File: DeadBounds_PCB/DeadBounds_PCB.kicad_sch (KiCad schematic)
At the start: 1 part

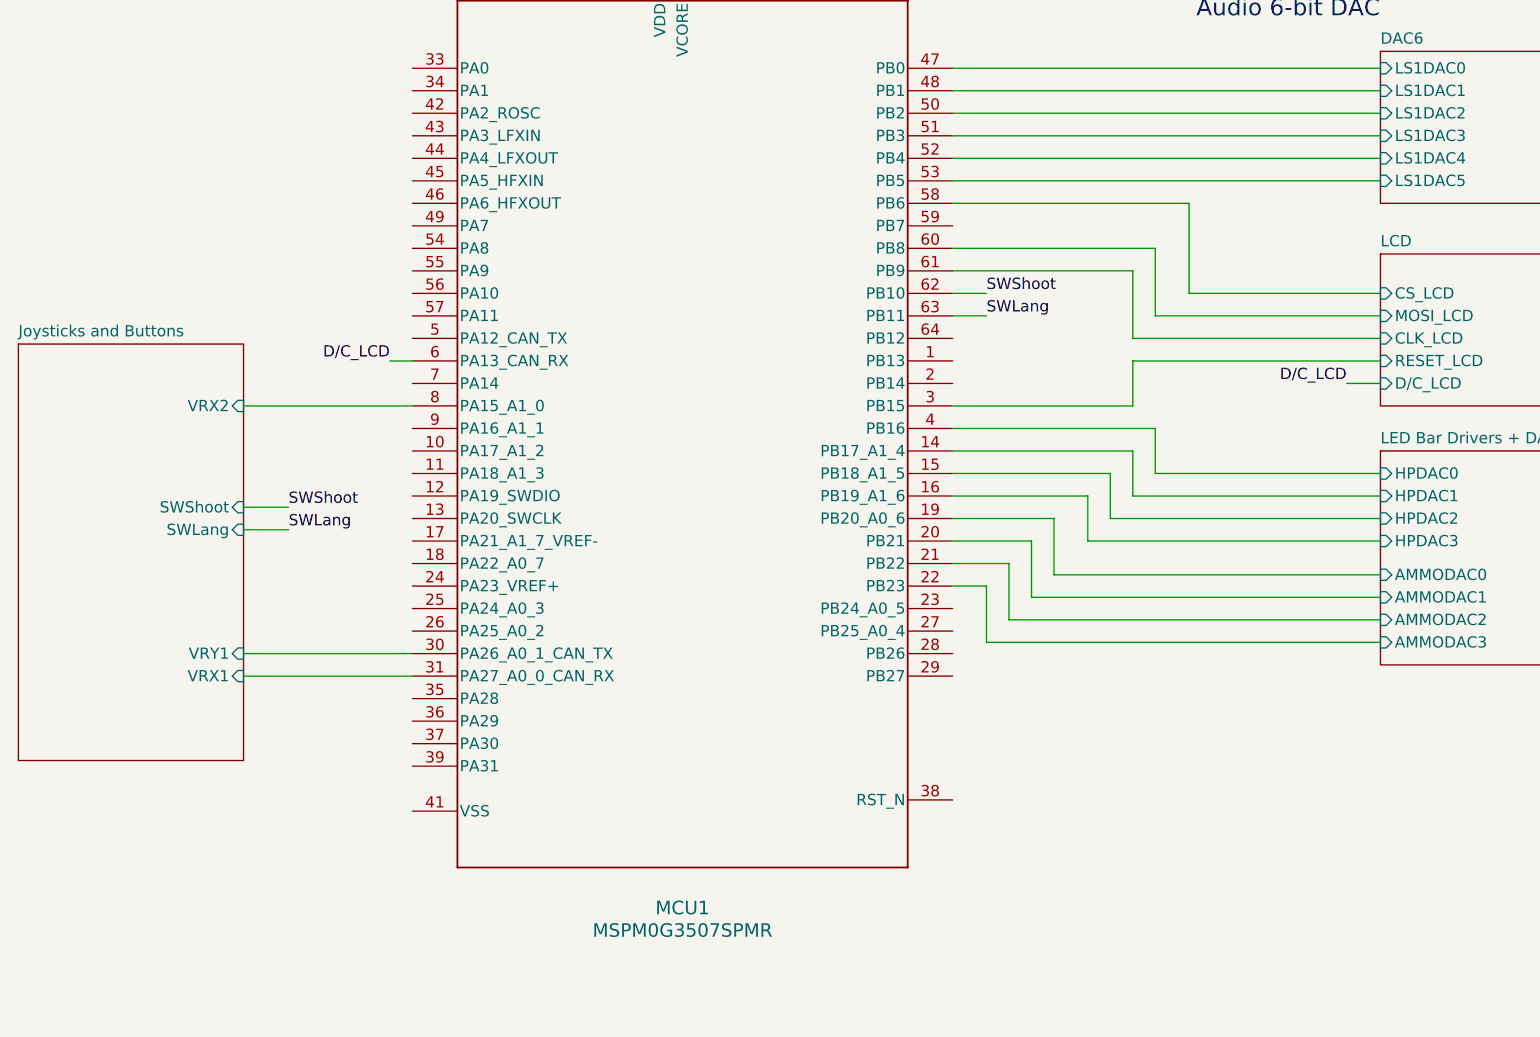
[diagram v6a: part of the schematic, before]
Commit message: Added amplifier circuit and additional jumpers to PCB
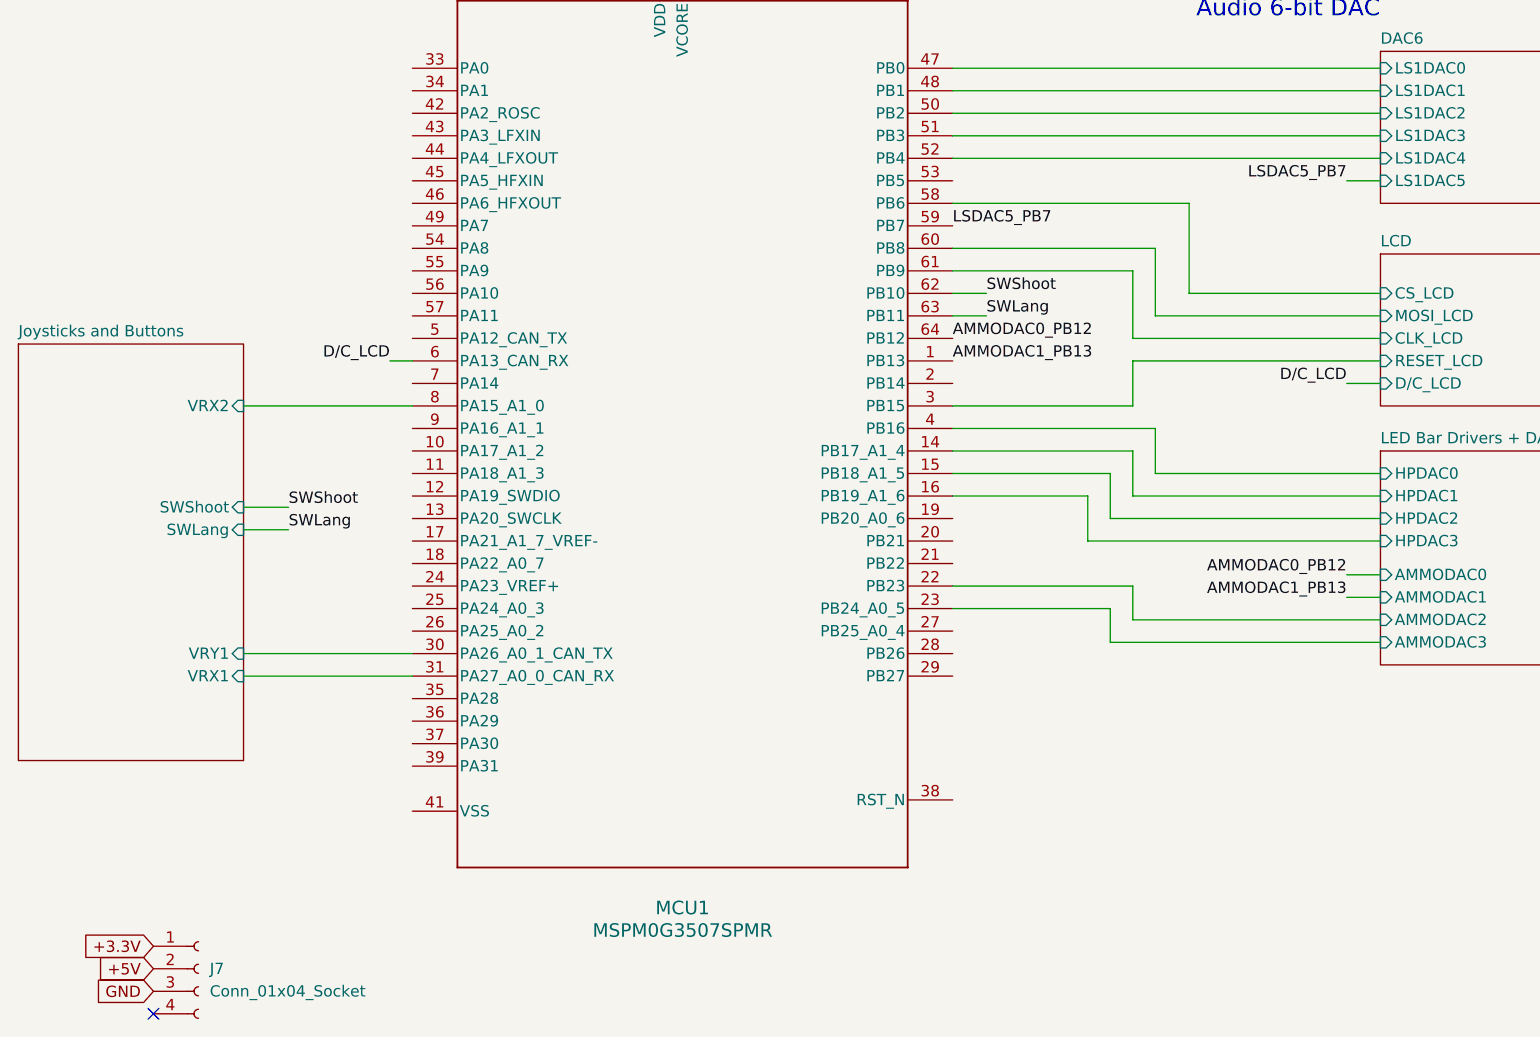
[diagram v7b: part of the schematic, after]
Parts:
- added J7: Conn_01x04_Socket, Connector_PinSocket_2.54mm:PinSocket_1x04_P2.54mm_Horizontal, symbol Connector:Conn_01x04_Socket
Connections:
- net LED Bar Drivers + DAC4s/AMMODAC2: now also MCU1.22 (PB23); no longer MCU1.21 (PB22)
- net LED Bar Drivers + DAC4s/AMMODAC3: now also MCU1.23 (PB24_A0_5); no longer MCU1.22 (PB23)
- net AMMODAC1_PB13: now reaches MCU1.1 (PB13)
- net LSDAC5_PB7: now reaches MCU1.59 (PB7)
- net AMMODAC0_PB12: now reaches MCU1.64 (PB12)
- net DAC6/LS1DAC5: no longer names the net of MCU1.53 (PB5)
- net LED Bar Drivers + DAC4s/AMMODAC0: no longer names the net of MCU1.19 (PB20_A0_6)
- net LED Bar Drivers + DAC4s/AMMODAC1: no longer names the net of MCU1.20 (PB21)
- new net +3.3V: J7.1 (Pin_1)
- new net +5V: J7.2 (Pin_2)
- new net GND: J7.3 (Pin_3)
- no-connect marks 0 -> 1
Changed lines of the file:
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@@
 		)
+	)
+	(no_connect
+		(at 137.16 149.86)
 	)
 	(wire
@@
 	(wire
 		(pts
+			(xy 247.65 105.41) (xy 275.59 105.41)
+		)
+		(stroke
+			(width 0)
+			(type default)
+		)
+	)
+	(wire
+		(pts
 			(xy 245.11 93.98) (xy 275.59 93.98)
 		)
@@
 	(wire
 		(pts
-			(xy 231.14 101.6) (xy 231.14 107.95)
-		)
-		(stroke
-			(width 0)
-			(type default)
-		)
-	)
-	(wire
-		(pts
 			(xy 245.11 88.9) (xy 245.11 93.98)
 		)
@@
 	(wire
 		(pts
-			(xy 238.76 100.33) (xy 275.59 100.33)
-		)
-		(stroke
-			(width 0)
-			(type default)
-		)
-	)
-	(wire
-		(pts
 			(xy 250.19 83.82) (xy 250.19 88.9)
 		)
@@
 	(wire
 		(pts
+			(xy 271.78 102.87) (xy 275.59 102.87)
+		)
+		(stroke
+			(width 0)
+			(type default)
+		)
+	)
+	(wire
+		(pts
 			(xy 250.19 63.5) (xy 250.19 71.12)
 		)
@@
 	(wire
 		(pts
-			(xy 236.22 102.87) (xy 275.59 102.87)
+			(xy 271.78 100.33) (xy 275.59 100.33)
 		)
 		(stroke
@@
 	(wire
 		(pts
+			(xy 247.65 105.41) (xy 247.65 101.6)
+		)
+		(stroke
+			(width 0)
+			(type default)
+		)
+	)
+	(wire
+		(pts
 			(xy 163.83 76.2) (xy 166.37 76.2)
 		)
@@
 	(wire
 		(pts
-			(xy 238.76 93.98) (xy 238.76 100.33)
-		)
-		(stroke
-			(width 0)
-			(type default)
-		)
-	)
-	(wire
-		(pts
 			(xy 231.14 68.58) (xy 227.33 68.58)
 		)
@@
 	(wire
 		(pts
-			(xy 227.33 96.52) (xy 236.22 96.52)
+			(xy 245.11 104.14) (xy 245.11 107.95)
 		)
 		(stroke
@@
 	(wire
 		(pts
-			(xy 227.33 55.88) (xy 275.59 55.88)
+			(xy 227.33 104.14) (xy 245.11 104.14)
 		)
 		(stroke
@@
 	(wire
 		(pts
-			(xy 227.33 99.06) (xy 233.68 99.06)
-		)
-		(stroke
-			(width 0)
-			(type default)
-		)
-	)
-	(wire
-		(pts
 			(xy 247.65 73.66) (xy 247.65 66.04)
 		)
@@
 	(wire
 		(pts
-			(xy 231.14 107.95) (xy 275.59 107.95)
-		)
-		(stroke
-			(width 0)
-			(type default)
-		)
-	)
-	(wire
-		(pts
-			(xy 236.22 96.52) (xy 236.22 102.87)
+			(xy 245.11 107.95) (xy 275.59 107.95)
 		)
 		(stroke
@@
 	(wire
 		(pts
-			(xy 227.33 101.6) (xy 231.14 101.6)
-		)
-		(stroke
-			(width 0)
-			(type default)
-		)
-	)
-	(wire
-		(pts
-			(xy 233.68 99.06) (xy 233.68 105.41)
+			(xy 247.65 101.6) (xy 227.33 101.6)
 		)
 		(stroke
@@
 	(wire
 		(pts
-			(xy 233.68 105.41) (xy 275.59 105.41)
-		)
-		(stroke
-			(width 0)
-			(type default)
-		)
-	)
-	(wire
-		(pts
 			(xy 227.33 53.34) (xy 275.59 53.34)
 		)
@@
 	(wire
 		(pts
+			(xy 271.78 55.88) (xy 275.59 55.88)
+		)
+		(stroke
+			(width 0)
+			(type default)
+		)
+	)
+	(wire
+		(pts
 			(xy 227.33 63.5) (xy 250.19 63.5)
 		)
@@
 	(wire
 		(pts
-			(xy 227.33 93.98) (xy 238.76 93.98)
-		)
-		(stroke
-			(width 0)
-			(type default)
-		)
-	)
-	(wire
-		(pts
 			(xy 247.65 86.36) (xy 247.65 91.44)
 		)
@@
 			(width 0)
 			(type default)
+		)
+	)
+	(label "AMMODAC1_PB13"
+		(at 271.78 102.87 180)
+		(effects
+			(font
+				(size 1.27 1.27)
+			)
+			(justify right bottom)
+		)
+	)
+	(label "LSDAC5_PB7"
+		(at 227.33 60.96 0)
+		(effects
+			(font
+				(size 1.27 1.27)
+			)
+			(justify left bottom)
+		)
+	)
+	(label "AMMODAC0_PB12"
+		(at 227.33 73.66 0)
+		(effects
+			(font
+				(size 1.27 1.27)
+			)
+			(justify left bottom)
 		)
 	)
@@
 		)
 	)
+	(label "AMMODAC0_PB12"
+		(at 271.78 100.33 180)
+		(effects
+			(font
+				(size 1.27 1.27)
+			)
+			(justify right bottom)
+		)
+	)
 	(label "SWLang"
 		(at 152.4 95.25 0)
@@
 		)
 	)
+	(label "AMMODAC1_PB13"
+		(at 227.33 76.2 0)
+		(effects
+			(font
+				(size 1.27 1.27)
+			)
+			(justify left bottom)
+		)
+	)
+	(label "LSDAC5_PB7"
+		(at 271.78 55.88 180)
+		(effects
+			(font
+				(size 1.27 1.27)
+			)
+			(justify right bottom)
+		)
+	)
 	(label "SWShoot"
 		(at 152.4 92.71 0)
@@
 		)
 	)
+	(global_label "GND"
+		(shape input)
+		(at 137.16 147.32 180)
+		(fields_autoplaced yes)
+		(effects
+			(font
+				(size 1.27 1.27)
+			)
+			(justify right)
+		)
+		(property "Intersheetrefs" "${INTERSHEET_REFS}"
+			(at 130.3043 147.32 0)
+			(hide yes)
+			(show_name no)
+			(do_not_autoplace no)
+			(effects
+				(font
+					(size 1.27 1.27)
+				)
+				(justify right)
+			)
+		)
+	)
+	(global_label "+3.3V"
+		(shape input)
+		(at 137.16 142.24 180)
+		(fields_autoplaced yes)
+		(effects
+			(font
+				(size 1.27 1.27)
+			)
+			(justify right)
+		)
+		(property "Intersheetrefs" "${INTERSHEET_REFS}"
+			(at 128.49 142.24 0)
+			(hide yes)
+			(show_name no)
+			(do_not_autoplace no)
+			(effects
+				(font
+					(size 1.27 1.27)
+				)
+				(justify right)
+			)
+		)
+	)
+	(global_label "+5V"
+		(shape input)
+		(at 137.16 144.78 180)
+		(fields_autoplaced yes)
+		(effects
+			(font
+				(size 1.27 1.27)
+			)
+			(justify right)
+		)
+		(property "Intersheetrefs" "${INTERSHEET_REFS}"
+			(at 130.3043 144.78 0)
+			(hide yes)
+			(show_name no)
+			(do_not_autoplace no)
+			(effects
+				(font
+					(size 1.27 1.27)
+				)
+				(justify right)
+			)
+		)
+	)
+	(symbol
+		(lib_id "Connector:Conn_01x04_Socket")
+		(at 142.24 144.78 0)
+		(unit 1)
+		(body_style 1)
+		(exclude_from_sim no)
+		(in_bom yes)
+		(on_board yes)
+		(in_pos_files yes)
+		(dnp no)
+		(fields_autoplaced yes)
+		(property "Reference" "J7"
+			(at 143.51 144.7799 0)
+			(show_name no)
+			(do_not_autoplace no)
+			(effects
+				(font
+					(size 1.27 1.27)
+				)
+				(justify left)
+			)
+		)
+		(property "Value" "Conn_01x04_Socket"
+			(at 143.51 147.3199 0)
+			(show_name no)
+			(do_not_autoplace no)
+			(effects
+				(font
+					(size 1.27 1.27)
+				)
+				(justify left)
+			)
+		)
+		(property "Footprint" "Connector_PinSocket_2.54mm:PinSocket_1x04_P2.54mm_Horizontal"
+			(at 142.24 144.78 0)
+			(hide yes)
+			(show_name no)
+			(do_not_autoplace no)
+			(effects
+				(font
+					(size 1.27 1.27)
+				)
+			)
+		)
+		(property "Datasheet" ""
+			(at 142.24 144.78 0)
+			(hide yes)
+			(show_name no)
+			(do_not_autoplace no)
+			(effects
+				(font
+					(size 1.27 1.27)
+				)
+			)
+		)
+		(property "Description" "Generic connector, single row, 01x04, script generated"
+			(at 142.24 144.78 0)
+			(hide yes)
+			(show_name no)
+			(do_not_autoplace no)
+			(effects
+				(font
+					(size 1.27 1.27)
+				)
+			)
+		)
+		(pin "2"
+		)
+		(pin "1"
+		)
+		(pin "3"
+		)
+		(pin "4"
+		)
+		(instances
+			(project "DeadBounds_PCB"
+				(path "/c652495f-dd42-4f45-9891-1e05b67942c0"
+					(reference "J7")
+					(unit 1)
+				)
+			)
+		)
+	)

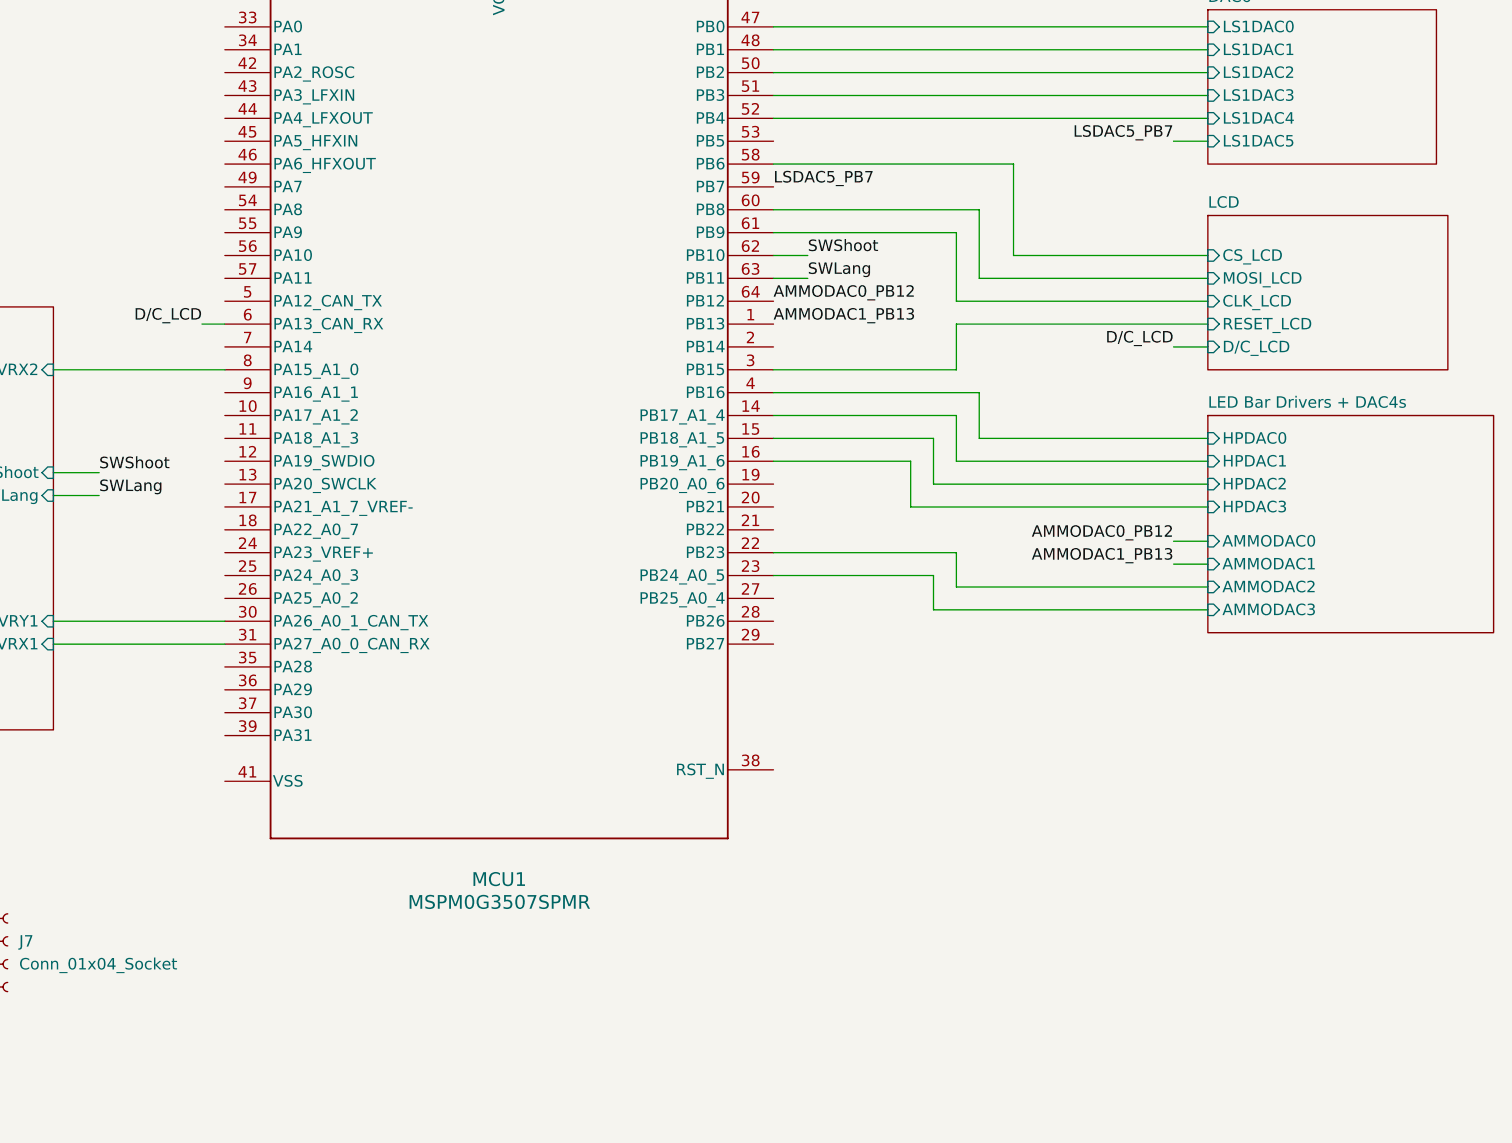
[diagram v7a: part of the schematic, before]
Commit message: Added mounting holes and rerouted around joystick. PCB Ordered
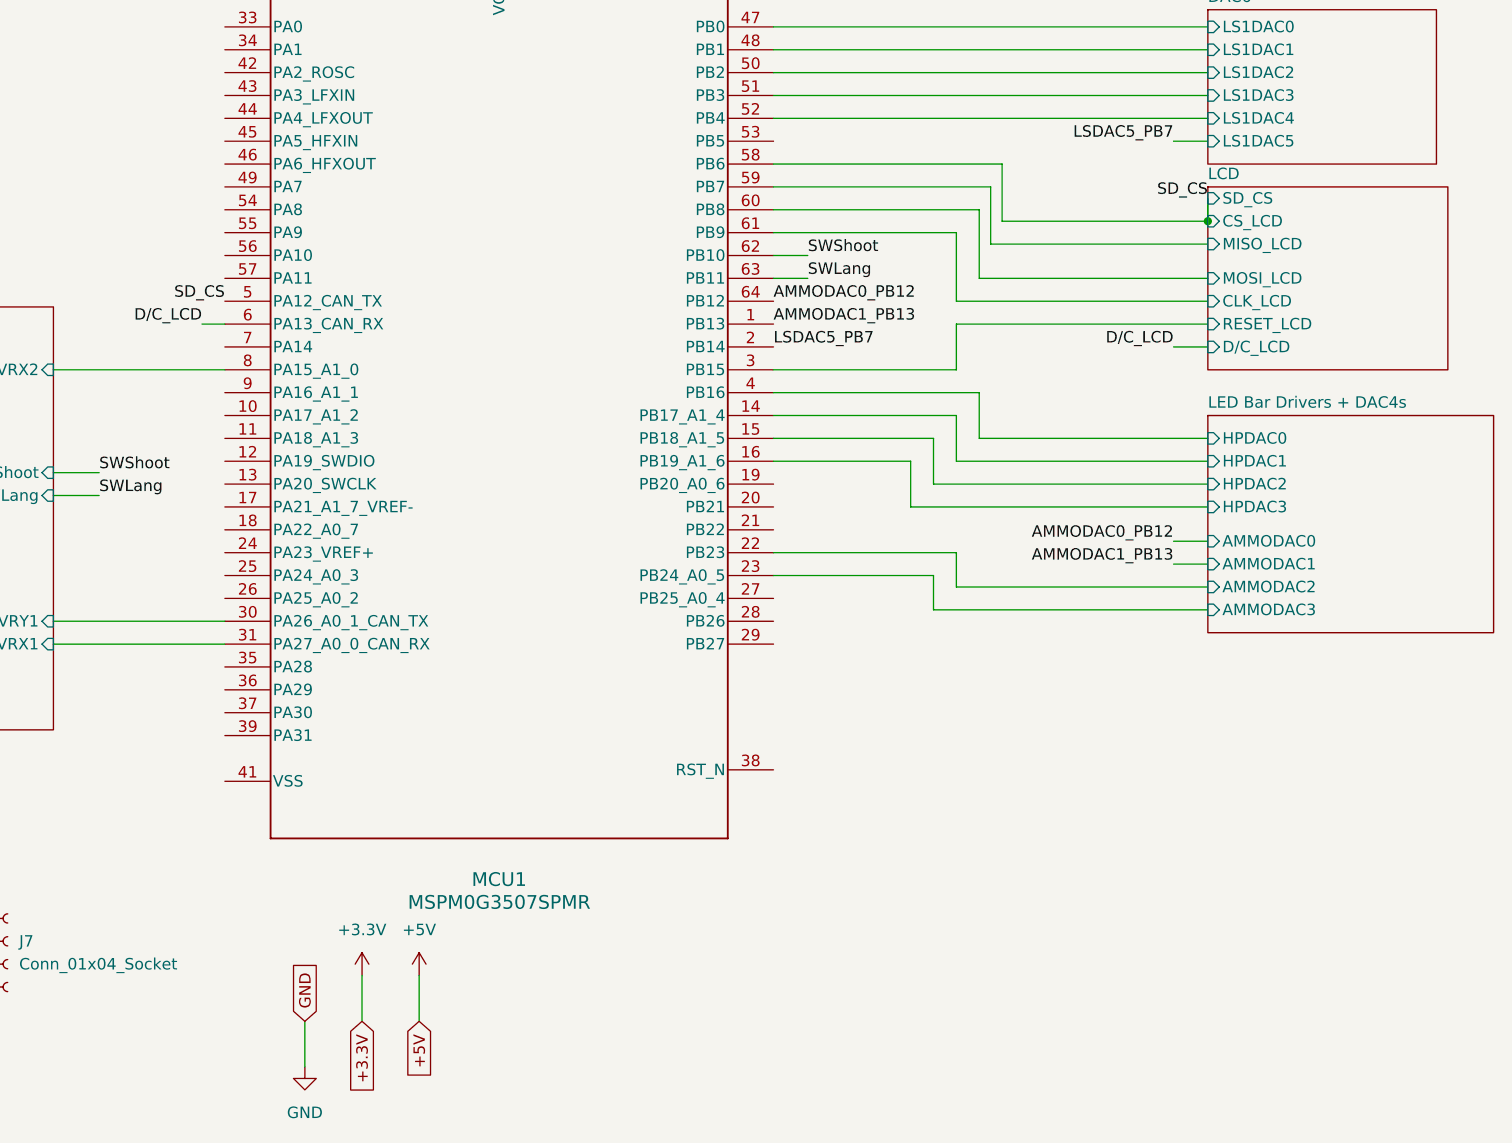
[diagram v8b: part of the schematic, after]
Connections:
- net LCD/CS_LCD is gone; now on net SD_CS: MCU1.58 (PB6)
- net LSDAC5_PB7: now also MCU1.2 (PB14); no longer MCU1.59 (PB7)
- net SD_CS: now reaches MCU1.5 (PA12_CAN_TX)
- new net LCD/MISO_LCD: MCU1.59 (PB7)
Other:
- sheet LCD ports: added MISO_LCD, SD_CS; removed none
